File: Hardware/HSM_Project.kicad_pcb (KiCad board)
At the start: 2 copper layers, 97 x 111.3 mm, 105 parts, among them J1 Conn_01x02_Pin, J10 VL530X Connector, J11 VL530X Connector, J12 VL530X Connector, J13 VL530X Connector, J14 BNO085 Breakout, J16 HC-05 Breakout Board, J2 MP1584 Breakout, J4 TEENSY_4.1, J5 Conn_01x08_Pin, J6 Conn_01x06_Pin, J7 Conn_01x06_Pin, J8 VL530X Connector, J9 VL530X Connector, Q10 Q_NMOS_GSD, Q11 Q_NMOS_GSD, Q12 Q_NMOS_GSD, Q13 TEFT4300, Q2 Q_NMOS_GSD, Q3 TEFT4300, Q4 TEFT4300, Q5 TEFT4300, Q6 TEFT4300, Q7 TEFT4300, Q8 Q_NMOS_GSD, Q9 Q_NMOS_GSD, SW2 SW_SPDT, SW3 SW_Push, SW4 SW_Push, SW5 SW_SPDT

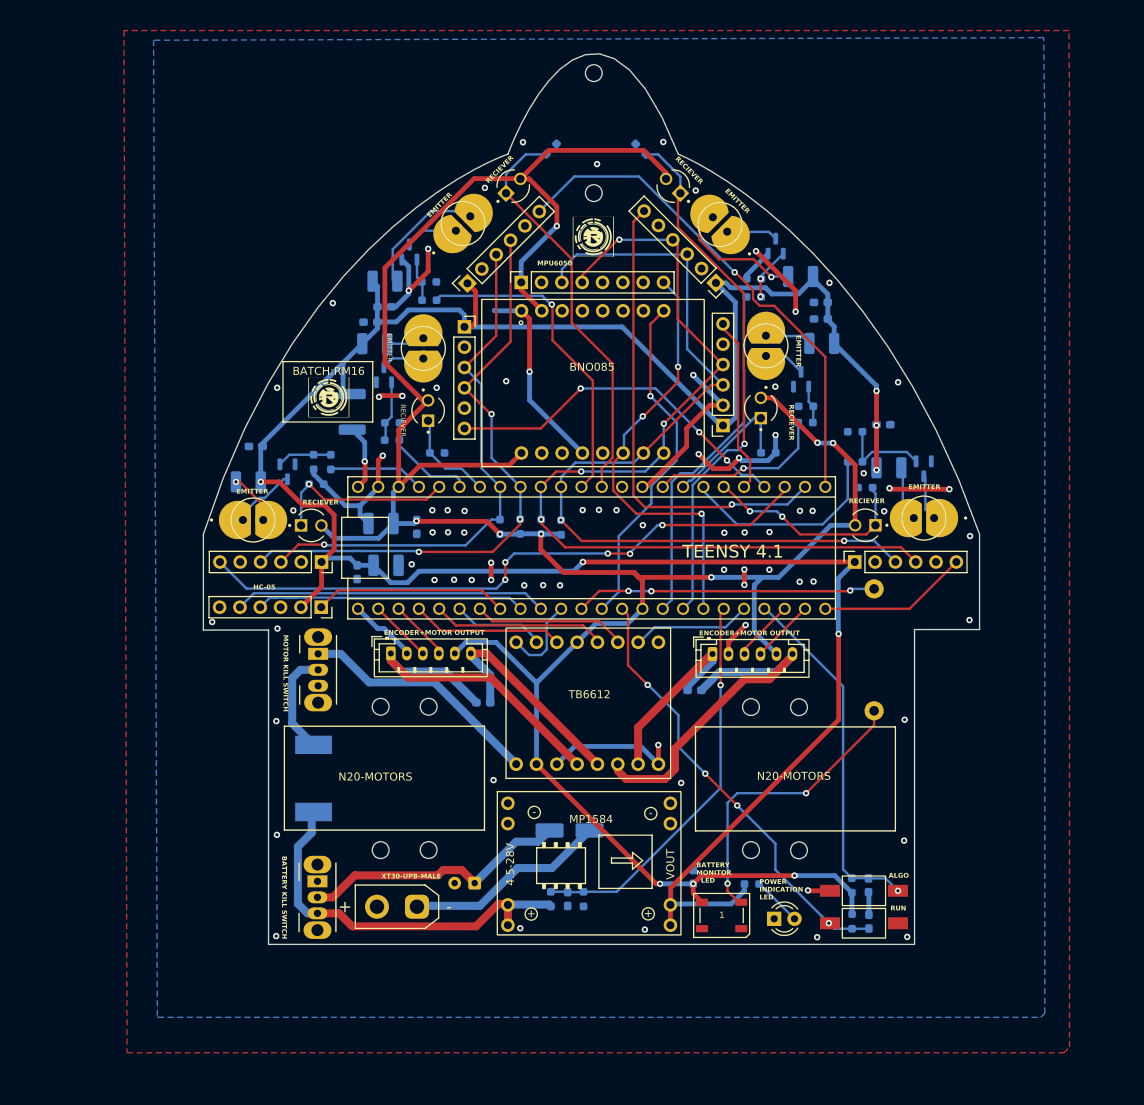
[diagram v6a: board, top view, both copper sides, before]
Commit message: Updated PCB files after dfm check
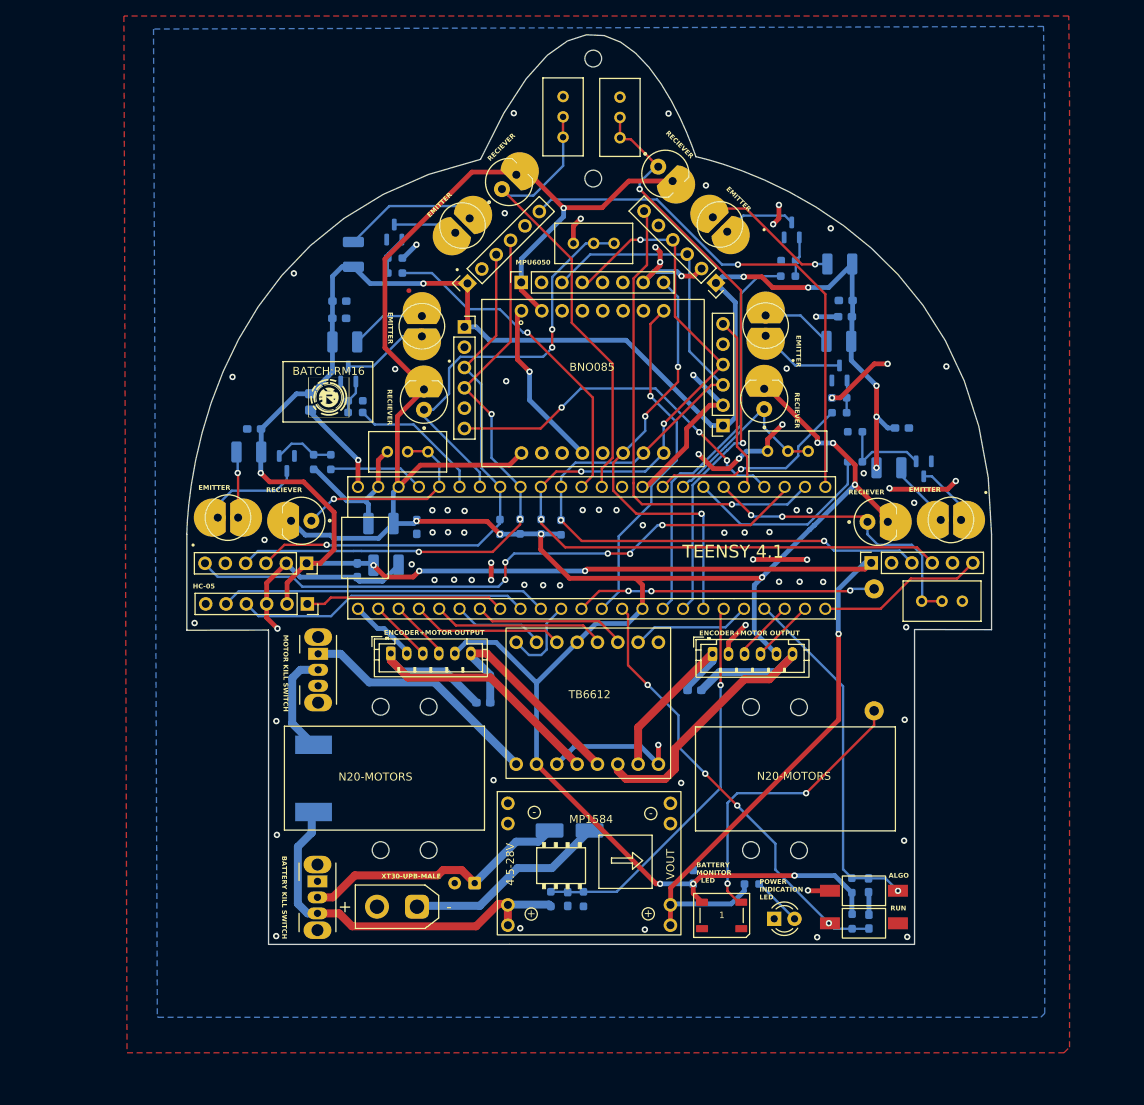
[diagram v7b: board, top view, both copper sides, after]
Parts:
- removed the G*** at (153.8, 42.8)
- removed R10, R11, R12, R13, R14, R31: 10k, Resistor_SMD:R_0603_1608Metric_Pad0.98x0.95mm_HandSolder
- added RV1: R_Potentiometer_Trim, Potentiometer_THT:Potentiometer_Bourns_3296W_Vertical, F.Cu at (194.8, 88.4)
- added RV2: R_Potentiometer_Trim, Potentiometer_THT:Potentiometer_Bourns_3296W_Vertical, F.Cu at (150.0, 30.4)
- added RV3: R_Potentiometer_Trim, Potentiometer_THT:Potentiometer_Bourns_3296W_Vertical, F.Cu at (157.1, 30.5)
- added RV4: R_Potentiometer_Trim, Potentiometer_THT:Potentiometer_Bourns_3296W_Vertical, F.Cu at (180.6, 69.6)
- added RV5: R_Potentiometer_Trim, Potentiometer_THT:Potentiometer_Bourns_3296W_Vertical, F.Cu at (156.3, 43.7)
- added RV6: R_Potentiometer_Trim, Potentiometer_THT:Potentiometer_Bourns_3296W_Vertical, F.Cu at (133.1, 69.7)
- D1, D4, D6, D7, D8, D9: value SFH_4545 -> SFH_4550; footprint SFH_4545:DIO_SFH_4545 -> SFH_4550:DIO_SFH_4550
- F3: footprint Fuse:Fuse_1812_4532Metric_Pad1.30x3.40mm_HandSolder -> Fuse:Fuse_0805_2012Metric_Pad1.15x1.40mm_HandSolder
- Q13, Q3, Q4, Q5, Q6, Q7: value TEFT4300 -> SFH_313_FA-3_4; footprint TEFT4300 (2):XDCR_TEFT4300 -> SFH_313_FA-3_4:XDCR_SFH_313_FA-3_4
- moved R21 5.74 mm to (124.0, 64.8)
- moved C2 5.68 mm to (122.0, 50.9)
- moved R15 5.47 mm to (129.0, 47.4)
- moved R37 5.35 mm to (124.0, 63.3)
- moved F3 5.35 mm to (118.4, 63.5)
- moved R34 5.19 mm to (129.0, 45.5)
- moved R16 5.18 mm to (123.8, 45.0), turned to 90 degrees
- moved R18 5.14 mm to (184.6, 46.2)
- moved R17 5.01 mm to (178.1, 47.8)
- moved R35 4.87 mm to (178.2, 45.8)
- moved Q10 4.86 mm to (184.5, 59.9)
- moved Q11 4.46 mm to (123.1, 60.0)
- moved R19 4.40 mm to (184.5, 64.8)
- moved R36 4.30 mm to (184.5, 63.0)
- moved C12 3.93 mm to (122.0, 53.0), turned to 0 degrees
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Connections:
- R16 pad 2: Net-(D1-Pad2) -> Net-(D1-PadA)
- R18 pad 2: Net-(D6-Pad2) -> Net-(D6-PadA)
- R20 pad 2: Net-(D7-Pad2) -> Net-(D7-PadA)
- R22 pad 2: Net-(D8-Pad2) -> Net-(D8-PadA)
- R29 pad 2: Net-(D9-Pad2) -> Net-(D9-PadA)
- R8 pad 2: Net-(D4-Pad2) -> Net-(D4-PadA)
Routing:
- net /Control Unit/SENS_LEFT: track 12.1 -> 52.3 mm, vias 0 -> 2
- net GND: track 155.2 -> 187.5 mm
- net Net-(D1-PadA): track 0.00 -> 18.3 mm
- net Net-(D6-PadA): track 0.00 -> 17.7 mm, vias 0 -> 1
- net Net-(D6-Pad2): track 16.5 -> 0.00 mm, vias 1 -> 0
- net Net-(D1-Pad2): track 16.4 -> 0.00 mm
- net +5V: track 314.7 -> 326.1 mm, vias 6 -> 11
- net /Control Unit/SENS_FRONT: track 26.9 -> 37.8 mm
- net Net-(D8-PadA): track 0.00 -> 9.42 mm
- net Net-(D7-PadA): track 0.00 -> 8.94 mm
- net Net-(D9-PadA): track 0.00 -> 8.49 mm, vias 0 -> 1
- net /Control Unit/SENS_FRONT_LEFT: track 51.2 -> 59.2 mm
- net Net-(D4-PadA): track 0.00 -> 7.65 mm
- net /Control Unit/SENS_FRONT_RIGHT: track 67.0 -> 74.3 mm, vias 1 -> 2
- net Net-(D9-Pad2): track 6.47 -> 0.00 mm, vias 1 -> 0
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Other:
- board size 97 x 111.3 mm -> 100.6 x 113.7 mm

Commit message: Made changes with i2c bus, added state connection and removed en of hc05, added bno085 fuse,bno085 2nd 3v3 unconnected flag has been put, reversed the connection for battery connector based on the xt30 signs,removed all daisy chained power traces and made it into start topology, fiexd drc erros,dfm check erros
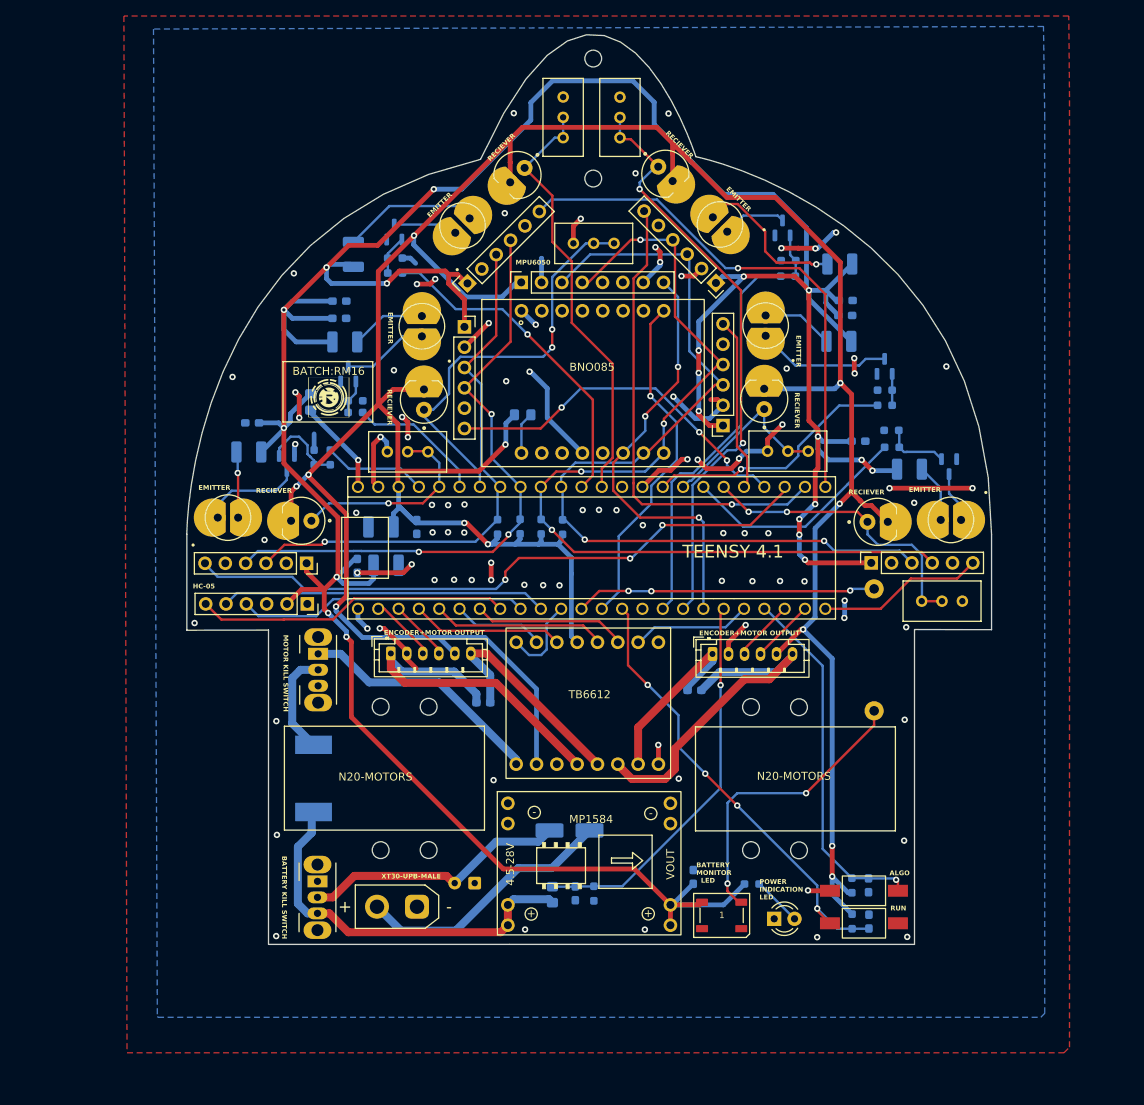
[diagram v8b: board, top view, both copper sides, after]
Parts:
- added F1: Polyfuse, Fuse:Fuse_0805_2012Metric_Pad1.15x1.40mm_HandSolder, B.Cu at (144.9, 65.1)
- R6: value 20k -> 30k; footprint Resistor_SMD:R_0603_1608Metric_Pad0.98x0.95mm_HandSolder -> Resistor_SMD:R_0805_2012Metric_Pad1.20x1.40mm_HandSolder
- moved R36 5.77 mm to (190.2, 62.0)
- moved R19 5.77 mm to (190.2, 63.9)
- moved Q10 5.70 mm to (190.2, 59.0)
- moved C1 5.68 mm to (186.9, 68.4)
- moved R9 4.95 mm to (191.1, 69.2)
- moved R32 4.55 mm to (191.0, 67.0)
- moved Q2 3.18 mm to (198.2, 71.6)
- moved R8 2.58 mm to (193.3, 71.9)
- moved R7 1.47 mm to (153.8, 124.9)
- moved Q4 1.34 mm to (144.3, 35.1), turned to -135 degrees
- moved C8 1.19 mm to (151.5, 124.9)
- moved Q9 1.18 mm to (177.4, 41.7)
- moved C13 0.80 mm to (111.1, 66.1)
- moved R6 0.59 mm to (148.7, 125.1)
- moved R38 0.59 mm to (118.9, 70.4), turned to 90 degrees
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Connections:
- C10 pad 1: Net-(D2-K) -> GND
- C10 pad 2: GND -> Net-(D2-K)
- C9 pad 1: +3.3V -> +5V
- D5 pad 1: +3.3V -> +5V
- J1 pad 1: Net-(D2-A) -> GND
- J1 pad 2: GND -> Net-(D2-A)
- J14 pad 16: +3.3V -> Net-(F1-Pad1)
- J14 pad 2: +3.3V -> unconnected-(J14-3V3-Pad2)
- J16 pad 1: /Control Unit/AT_COMMAND_LINE -> unconnected-(J16-EN-Pad1)
- J16 pad 6: unconnected-(J16-STATE-Pad6) -> /Control Unit/STATE_HC-05
- J4 pad 3V3@2: +3.3V -> unconnected-(J4-3.3V-Pad3V3@2)
- J4 pad D6: /Control Unit/AT_COMMAND_LINE -> /Control Unit/STATE_HC-05
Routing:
- net +5V: track 326.1 -> 427.5 mm, vias 11 -> 20
- net +3.3V: track 330.6 -> 394.4 mm, vias 11 -> 12
- net GND: track 187.5 -> 141.4 mm, vias 77 -> 87
- net /Control Unit/STATE_HC-05: track 0.00 -> 39.2 mm
- net /Control Unit/AT_COMMAND_LINE: track 25.0 -> 0.00 mm
- net Net-(D2-A): track 25.5 -> 33.0 mm
- net /Control Unit/EMITTER_RIGHT: track 25.7 -> 31.8 mm
- net Net-(Q10-D): track 10.8 -> 16.7 mm
- net Net-(F1-Pad1): track 0.00 -> 5.27 mm
- net /Control Unit/SENS_FRONT_LEFT: track 59.2 -> 54.1 mm
- net /Control Unit/EMITTER_FRONT: track 24.9 -> 28.8 mm
- net Net-(Q2-G): track 11.5 -> 8.05 mm
- net Net-(Q12-G): track 7.65 -> 10.3 mm
- net /Control Unit/RUN_MODE_GPIO: track 55.7 -> 57.7 mm
- net Net-(D6-PadA): track 17.7 -> 19.6 mm
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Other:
- board text added: "DNP"
